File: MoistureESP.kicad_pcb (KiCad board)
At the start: 2 copper layers, 104 parts, among them J1 Conn_01x03_Pin, J2 Conn_MoisturePCB, J3 Conn_DS18B20, J4 USB4110-GF-A, J6 Conn_01x02_Pin, J7 Conn_01x06_Pin, Q1 SSM6K513NU-LF, Q10 DMP3068L-7, Q2 SSM6K513NU-LF, Q3 2N7002W, Q4 BC817W, Q5 BC817W, Q6 RUM002N05T2L, Q7 RUM002N05T2L, Q8 DMP3068L-7, Q9 DMP3068L-7, SW1 147873-1, U1 BQ28Z620DRZR, U2 ESP32-WROOM-32, U3 TPS7A2601DRVR, U4 TPS7A2601DRVR, U5 MAX77757JEFG420+

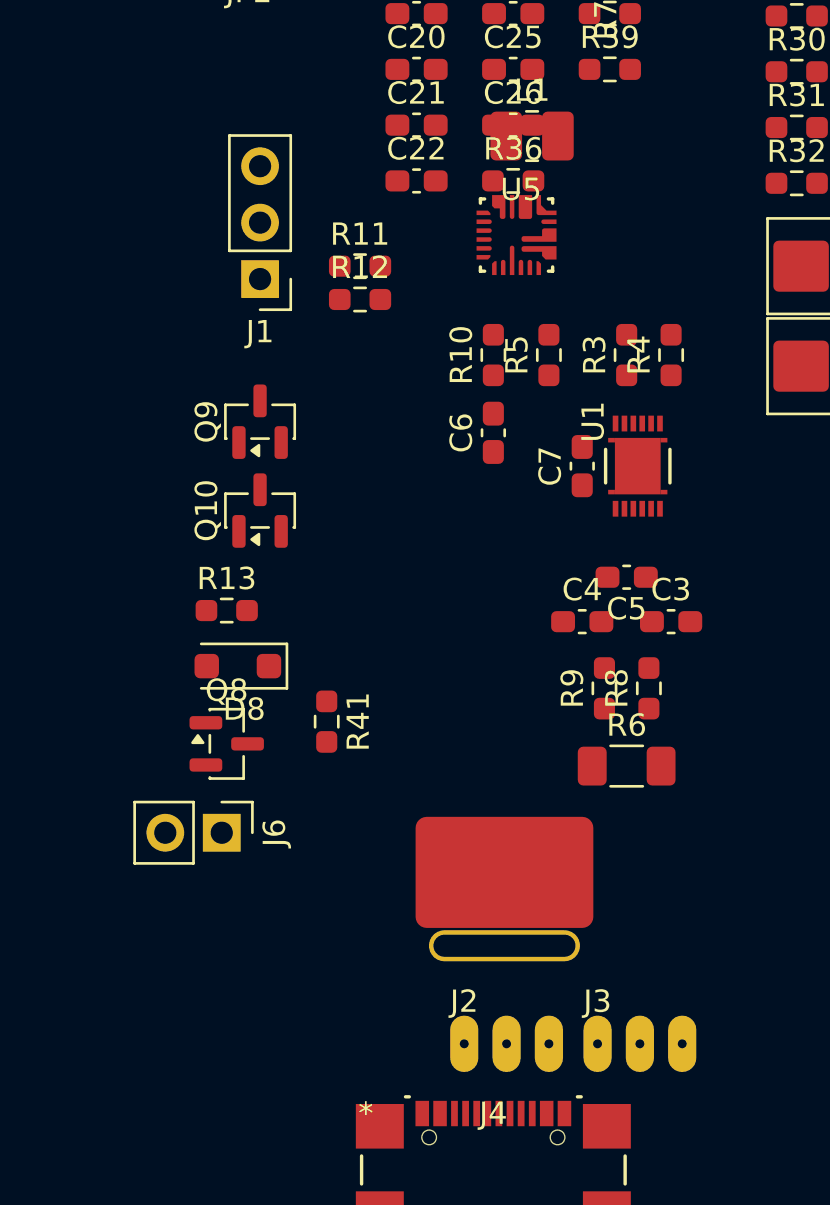
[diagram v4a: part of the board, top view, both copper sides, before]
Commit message: Change protection FETs and add resistor.
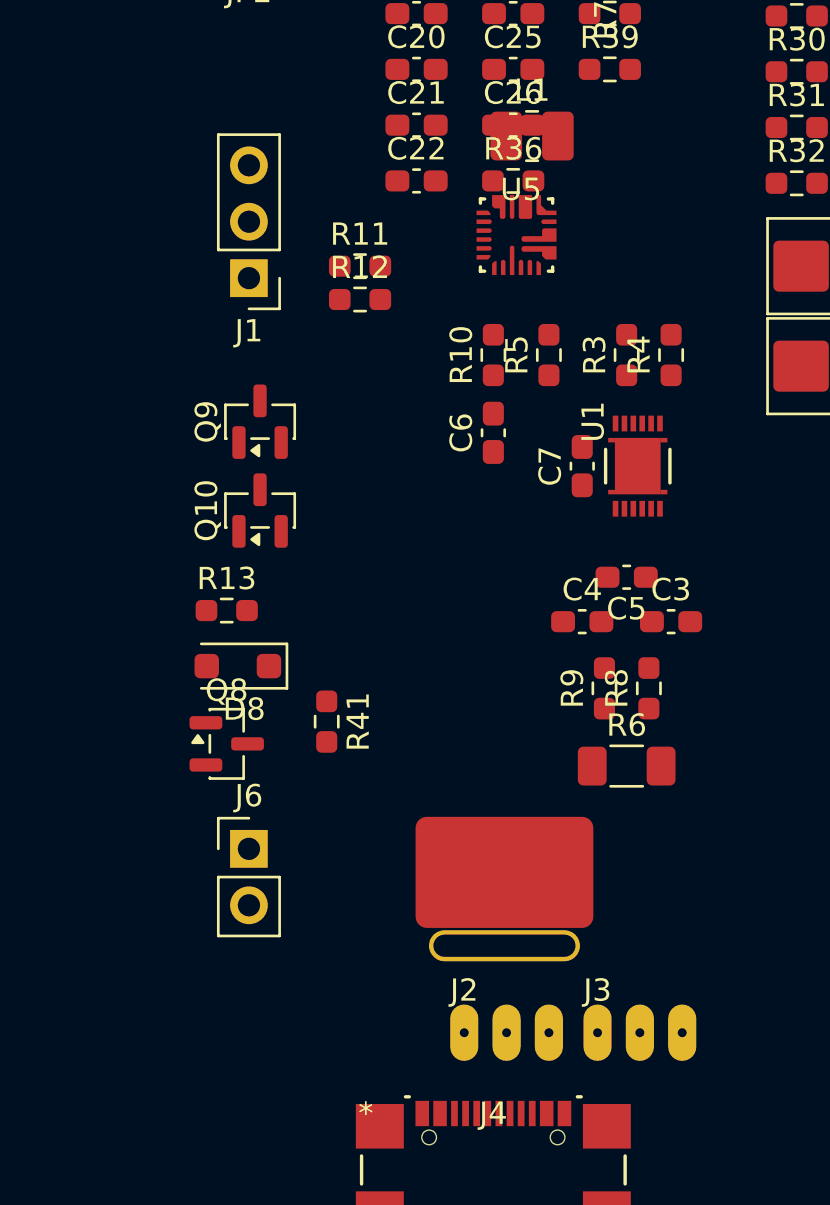
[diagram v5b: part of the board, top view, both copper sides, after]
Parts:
- moved J6 1.42 mm to (73.5, 125.7), turned to 0 degrees
- moved J1 0.50 mm to (73.5, 100.0)
- moved J2 0.50 mm to (83.2, 134.0)
- moved J3 0.50 mm to (89.2, 134.0)
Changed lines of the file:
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@@
 	(footprint "custom:sensorwirepads3x1"
 		(layer "F.Cu")
-		(at 83.19 134.5)
+		(at 83.19 134)
 		(property "Reference" "J2"
 			(at 0 -1.905 0)
@@
 	(footprint "Connector_PinHeader_2.54mm:PinHeader_1x02_P2.54mm_Vertical"
 		(layer "F.Cu")
-		(at 72.275 125 -90)
+		(at 73.5 125.725)
 		(descr "Through hole straight pin header, 1x02, 2.54mm pitch, single row")
 		(tags "Through hole pin header THT 1x02 2.54mm single row")
 		(property "Reference" "J6"
-			(at 0 -2.38 90)
+			(at 0 -2.38 0)
 			(layer "F.SilkS")
 			(effects
@@
 		)
 		(property "Value" "Conn_01x02_Pin"
-			(at 0 4.92 90)
+			(at 0 4.92 0)
 			(layer "F.Fab")
 			(effects
@@
 		)
 		(property "Datasheet" ""
-			(at 0 0 90)
+			(at 0 0 0)
 			(layer "F.Fab")
 			(hide yes)
@@
 		)
 		(property "Description" "Generic connector, single row, 01x02, script generated"
-			(at 0 0 90)
+			(at 0 0 0)
 			(layer "F.Fab")
 			(hide yes)
@@
 		)
 		(property "KiLib_Generator" "connector/pin_header_socket"
-			(at 0 0 90)
+			(at 0 0 0)
 			(layer "F.SilkS")
 			(hide yes)
@@
 		(duplicate_pad_numbers_are_jumpers no)
 		(fp_line
-			(start -1.38 3.92)
-			(end 1.38 3.92)
+			(start -1.38 -1.38)
+			(end 0 -1.38)
 			(stroke
 				(width 0.12)
@@
 		)
 		(fp_line
-			(start -1.38 1.27)
-			(end -1.38 3.92)
+			(start -1.38 0)
+			(end -1.38 -1.38)
 			(stroke
 				(width 0.12)
@@
 		(fp_line
 			(start -1.38 1.27)
-			(end 1.38 1.27)
+			(end -1.38 3.92)
 			(stroke
 				(width 0.12)
@@
 		)
 		(fp_line
-			(start 1.38 1.27)
-			(end 1.38 3.92)
+			(start -1.38 1.27)
+			(end 1.38 1.27)
 			(stroke
 				(width 0.12)
@@
 		)
 		(fp_line
-			(start -1.38 0)
-			(end -1.38 -1.38)
+			(start -1.38 3.92)
+			(end 1.38 3.92)
 			(stroke
 				(width 0.12)
@@
 		)
 		(fp_line
-			(start -1.38 -1.38)
-			(end 0 -1.38)
+			(start 1.38 1.27)
+			(end 1.38 3.92)
 			(stroke
 				(width 0.12)
@@
 		)
 		(fp_line
-			(start -1.27 3.81)
-			(end -1.27 -0.635)
+			(start -1.27 -0.635)
+			(end -0.635 -1.27)
 			(stroke
 				(width 0.1)
@@
 		)
 		(fp_line
-			(start 1.27 3.81)
-			(end -1.27 3.81)
+			(start -1.27 3.81)
+			(end -1.27 -0.635)
 			(stroke
 				(width 0.1)
@@
 		)
 		(fp_line
-			(start -1.27 -0.635)
-			(end -0.635 -1.27)
+			(start -0.635 -1.27)
+			(end 1.27 -1.27)
 			(stroke
 				(width 0.1)
@@
 		)
 		(fp_line
-			(start -0.635 -1.27)
-			(end 1.27 -1.27)
+			(start 1.27 -1.27)
+			(end 1.27 3.81)
 			(stroke
 				(width 0.1)
@@
 		)
 		(fp_line
-			(start 1.27 -1.27)
-			(end 1.27 3.81)
+			(start 1.27 3.81)
+			(end -1.27 3.81)
 			(stroke
 				(width 0.1)
@@
 		)
 		(fp_text user "${REFERENCE}"
-			(at 0 1.27 0)
+			(at 0 1.27 90)
 			(layer "F.Fab")
 			(effects
@@
 		)
 		(pad "1" thru_hole rect
-			(at 0 0 270)
+			(at 0 0)
 			(size 1.7 1.7)
 			(drill 1)
@@
 		)
 		(pad "2" thru_hole circle
-			(at 0 2.54 270)
+			(at 0 2.54)
 			(size 1.7 1.7)
 			(drill 1)
@@
 	(footprint "custom:sensorwirepads3x1"
 		(layer "F.Cu")
-		(at 89.19 134.5)
+		(at 89.19 134)
 		(property "Reference" "J3"
 			(at 0 -1.905 0)
@@
 	(footprint "Connector_PinHeader_2.54mm:PinHeader_1x03_P2.54mm_Vertical"
 		(layer "F.Cu")
-		(at 74 100.08 180)
+		(at 73.5 100.04 180)
 		(descr "Through hole straight pin header, 1x03, 2.54mm pitch, single row")
 		(tags "Through hole pin header THT 1x03 2.54mm single row")

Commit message: Placement concept is finished.
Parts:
- added D3: LED, LED_SMD:LED_0603_1608Metric, B.Cu at (97.0, 69.0)
- added D4: LED, LED_SMD:LED_0603_1608Metric, B.Cu at (95.0, 69.0)
- added R42: 10K, Resistor_SMD:R_0603_1608Metric_Pad0.98x0.95mm_HandSolder, F.Cu at (75.0, 117.5)
- D5, R35, R40: moved to F.Cu
- D6, D7: value SM6T6V8A -> ESD5Zxx; footprint Diode_SMD:D_SMB -> Diode_SMD:D_SOD-523
- Q10: value DMP3068L-7 -> BC856BLT1G0SCT-ND
- Q8, Q9: value DMP3068L-7 -> SI7137DP-T1-GE3; footprint Package_TO_SOT_SMD:SOT-23 -> custom:MOSFET_7DP-T1-GE3_VIS
- moved D2 37.6 mm to (73.4, 66.5), turned to 180 degrees
- moved R32 35.7 mm to (73.5, 70.0), turned to -90 degrees
- moved R31 33.5 mm to (78.0, 66.5), turned to -90 degrees
- moved D1 31.4 mm to (76.5, 69.5), turned to 180 degrees
- moved R36 30.9 mm to (92.0, 65.5)
- moved C16 30.3 mm to (77.0, 64.0)
- moved R30 28.6 mm to (77.0, 71.5)
- moved R29 24.7 mm to (78.0, 74.0), turned to -90 degrees
- moved J1 24.2 mm to (96.0, 109.1)
- moved D5 24.0 mm to (96.5, 65.5), turned to 0 degrees
- moved R40 23.5 mm to (96.5, 67.5), turned to 0 degrees
- moved R12 19.6 mm to (95.0, 111.5), turned to 180 degrees
- moved R35 19.5 mm to (93.5, 70.5)
- moved R37 18.3 mm to (92.0, 67.5)
- moved R11 17.8 mm to (93.5, 109.0), turned to -90 degrees
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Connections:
- Q10 pad 2: Net-(Q10-S) -> Net-(Q10-E)
- Q10 pad 3: Net-(Q10-D) -> Net-(Q10-C)
- Q8 pad 1: GNDPWR -> Net-(Q10-E)
- Q8 pad 2: Net-(Q10-S) -> Net-(Q8-S-Pad2)
- Q8 pad 3: /auxchgr_prot/Vin+ -> Net-(Q8-S-Pad2)
- Q9 pad 1: Net-(Q10-D) -> Net-(Q10-E)
- Q9 pad 2: Net-(Q10-S) -> Net-(Q9-S-Pad2)
- Q9 pad 3: /charger/VBat -> Net-(Q9-S-Pad2)
- R13 pad 2: Net-(Q10-D) -> Net-(Q10-C)
- R41 pad 2: Net-(Q10-S) -> Net-(Q10-E)
- U2 pad 10: /mcu/onewire_pin -> unconnected-(U2-IO25-Pad10)
- U2 pad 11: /mcu/analog_enable -> /mcu/Disp.SDA
- U2 pad 12: unconnected-(U2-IO27-Pad12) -> /mcu/Disp.SCL
- U2 pad 23: /mcu/Disp.SDA -> /mcu/analog_enable
- U2 pad 24: /mcu/Disp.SCL -> /mcu/onewire_pin

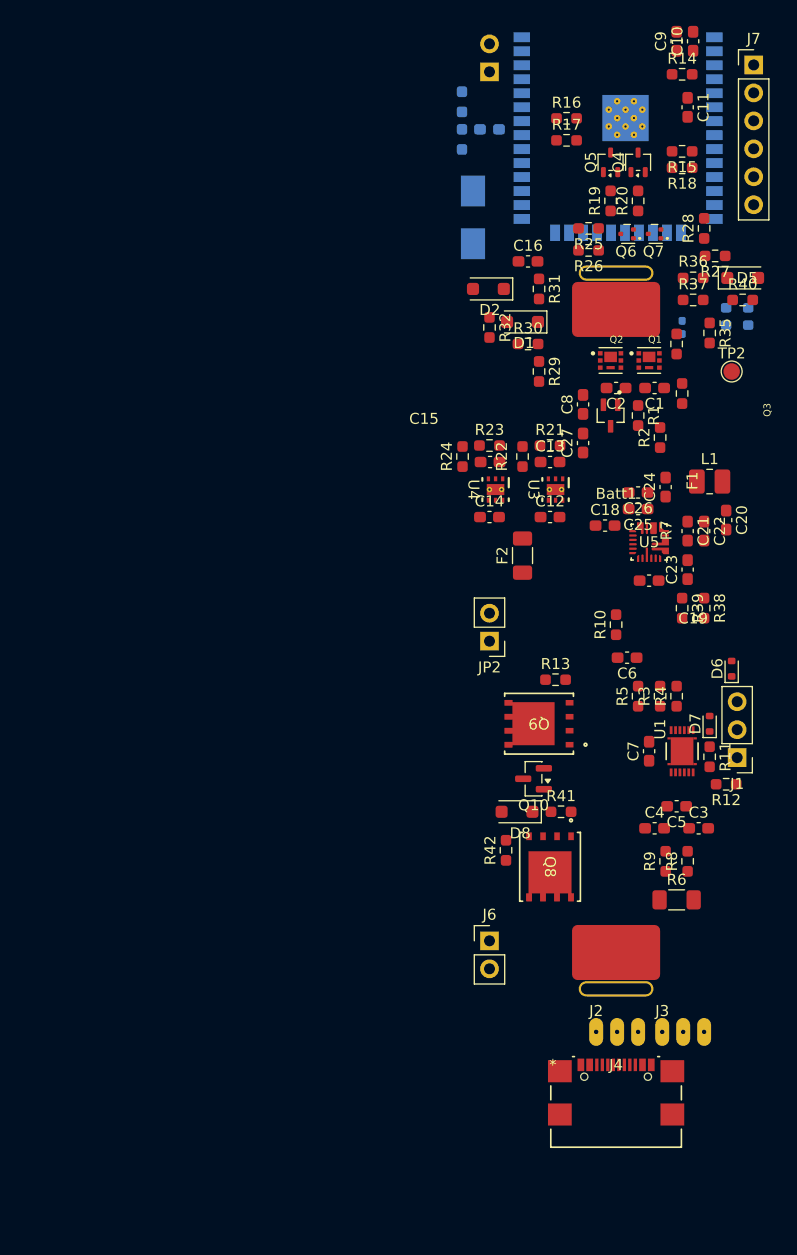
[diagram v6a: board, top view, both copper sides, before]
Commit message: Add wiring, change footprint to avoid fatal errors at pads.
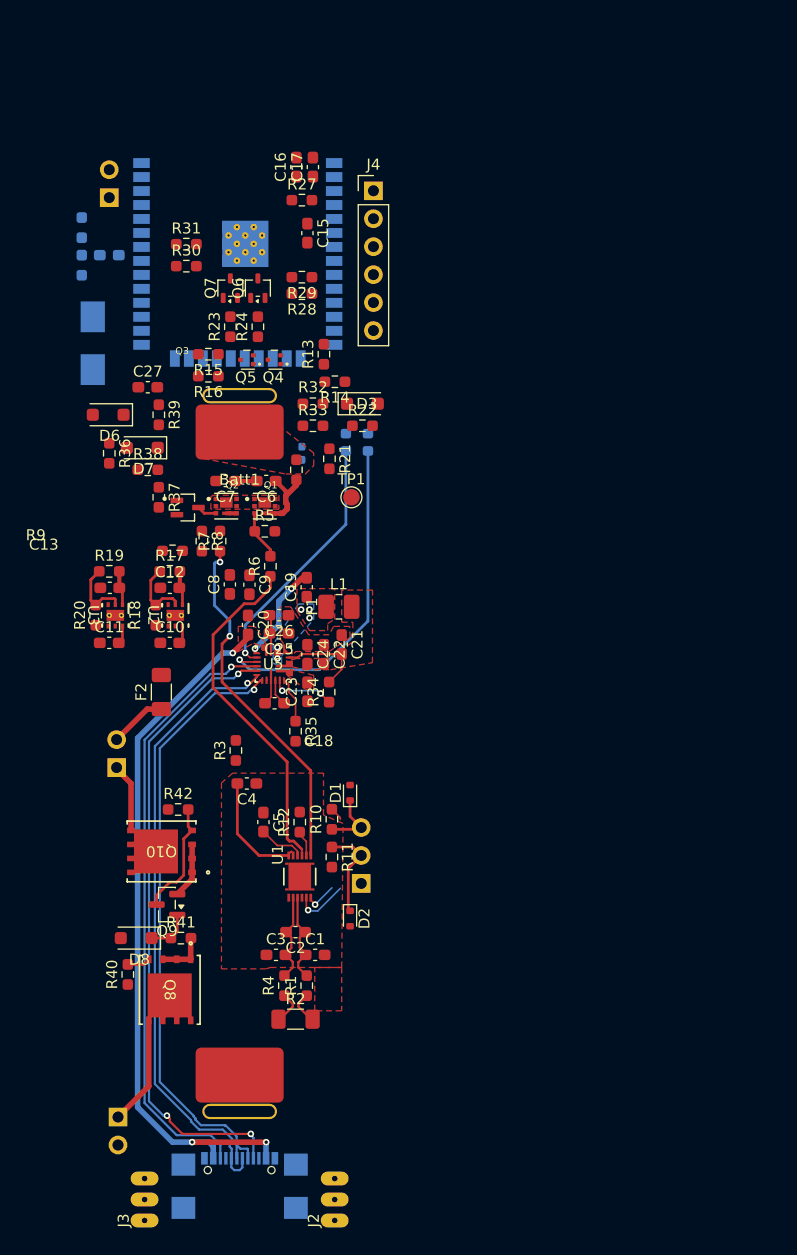
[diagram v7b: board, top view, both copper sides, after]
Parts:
- removed the Q9 at (78.0, 106.0)
- added Q10: SI7137DP-T1-GE3, custom:MOSFET_7DP-T1-GE3_VIS, F.Cu at (43.7, 117.6)
- J1: renamed from J6; moved to B.Cu
- J5: renamed from J1; moved to B.Cu
- J7: renamed from J4; moved to B.Cu
- JP1: renamed from JP2; moved to B.Cu
- moved J3 50.0 mm to (42.2, 151.1), turned to 90 degrees
- moved R9 48.5 mm to (44.7, 90.3), turned to 0 degrees
- moved R7 43.8 mm to (49.0, 89.4)
- moved R8 42.7 mm to (47.4, 89.4), turned to -90 degrees
- moved Q3 39.3 mm to (46.1, 86.4), turned to 0 degrees
- moved R35 38.8 mm to (55.9, 106.7)
- moved J1 37.4 mm to (39.8, 141.7), turned to 180 degrees
- moved Q1 37.3 mm to (53.1, 86.2)
- moved Q2 37.3 mm to (49.6, 86.2)
- moved R6 37.3 mm to (53.6, 91.7)
- moved D2 37.2 mm to (60.8, 123.7), turned to -90 degrees
- moved C21 36.7 mm to (60.1, 98.8)
- moved C1 36.7 mm to (57.7, 127.0)
- moved U1 36.6 mm to (56.3, 119.9)
- moved C7 36.5 mm to (49.5, 83.9)
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- renumbered C3 to C1, C12 to C10, C14 to C11, C13 to C12, C15 to C13, C17 to C14, C11 to C15, C9 to C16, C10 to C17, C19 to C18, C24 to C19, C5 to C2, C18 to C20, C20 to C21, C21 to C24, C16 to C27, C4 to C3, C6 to C4, C7 to C5, C1 to C6, C2 to C7, C27 to C9, D6 to D1, D7 to D2, D5 to D3, D3 to D4, D4 to D5, D2 to D6, D1 to D7, J7 to J4, JP1 to JP2, Q7 to Q4, Q6 to Q5, Q4 to Q6, Q5 to Q7, Q10 to Q9, R8 to R1, R11 to R10, R12 to R11, R5 to R12, R28 to R13, R27 to R14, R25 to R15, R26 to R16, R21 to R17, R22 to R18, R23 to R19, R6 to R2, R24 to R20, R35 to R21, R40 to R22, R19 to R23, R20 to R24, R33 to R25, R34 to R26, R14 to R27, R18 to R28, R15 to R29, R10 to R3, R17 to R30, R16 to R31, R36 to R32, R37 to R33, R39 to R34, R38 to R35, R32 to R36, R29 to R37, R30 to R38, R31 to R39, R9 to R4, R42 to R40, R13 to R42, R1 to R5, R3 to R6, R4 to R7, R2 to R8, R7 to R9, TP2 to TP1, U3 to U2, U4 to U3, U2 to U4
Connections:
- C19 pad 1: Net-(C24-Pad1) -> Net-(C19-Pad1)
- L1 pad 1: Net-(C24-Pad1) -> Net-(C19-Pad1)
- Q8 pad 1: Net-(Q10-E) -> Net-(Q9-E)
- Q8 pad 2: Net-(Q8-S-Pad2) -> Net-(Q9-E)
- Q8 pad 3: Net-(Q8-S-Pad2) -> Net-(Q9-E)
- Q8 pad 6: Net-(Q8-D-Pad6) -> /auxchgr_prot/Vin+
- Q8 pad 7: Net-(Q8-D-Pad6) -> /auxchgr_prot/Vin+
- Q8 pad 8: Net-(Q8-D-Pad6) -> /auxchgr_prot/Vin+
- Q9 pad 2: Net-(Q10-E) -> Net-(Q9-E)
- R41 pad 2: Net-(Q10-E) -> Net-(Q9-E)
- U5 pad 20: Net-(C24-Pad1) -> Net-(C19-Pad1)
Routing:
- net VBUS: track 0.00 -> 65.3 mm, vias 0 -> 3
- net /charger/CC1: track 0.00 -> 58.1 mm, vias 0 -> 3
- net /charger/DP1: track 0.00 -> 57.4 mm, vias 0 -> 1
- net /charger/DN1: track 0.00 -> 56.0 mm, vias 0 -> 1
- net /charger/CC2: track 0.00 -> 55.8 mm, vias 0 -> 1
- net Net-(U1-DSG): track 0.00 -> 32.3 mm, vias 0 -> 2
- net Net-(U1-CHG): track 0.00 -> 31.7 mm
- net Net-(D4-K): track 0.00 -> 31.0 mm, vias 0 -> 1
- net /charger/~{INOK}: track 0.00 -> 23.4 mm, vias 0 -> 1
- net Net-(U1-VC1): track 0.00 -> 11.0 mm
- net Net-(Q10-G): track 0.00 -> 10.5 mm
- net /auxchgr_prot/Vin+: track 0.00 -> 9.94 mm
- net Net-(Q9-E): track 0.00 -> 9.54 mm
- net Net-(U5-BST): track 0.00 -> 9.11 mm, vias 0 -> 2
- net /battery/comm.SDA: track 0.00 -> 8.73 mm
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- added copper zone on F.Cu, net /battery/Vcell+
- added copper zone on F.Cu, net /charger/VBat
- added copper zone on F.Cu, net CGND
- added copper zone on F.Cu, net GNDPWR
- added copper zone on B.Cu, net Net-(C19-Pad1)
- added copper zone on F.Cu, net Net-(C19-Pad1)
- added copper zone on F.Cu, net Net-(Q1-Pad1)
- added copper zone on F.Cu, net VBUS
- added copper zone on F.Cu, net Vsys

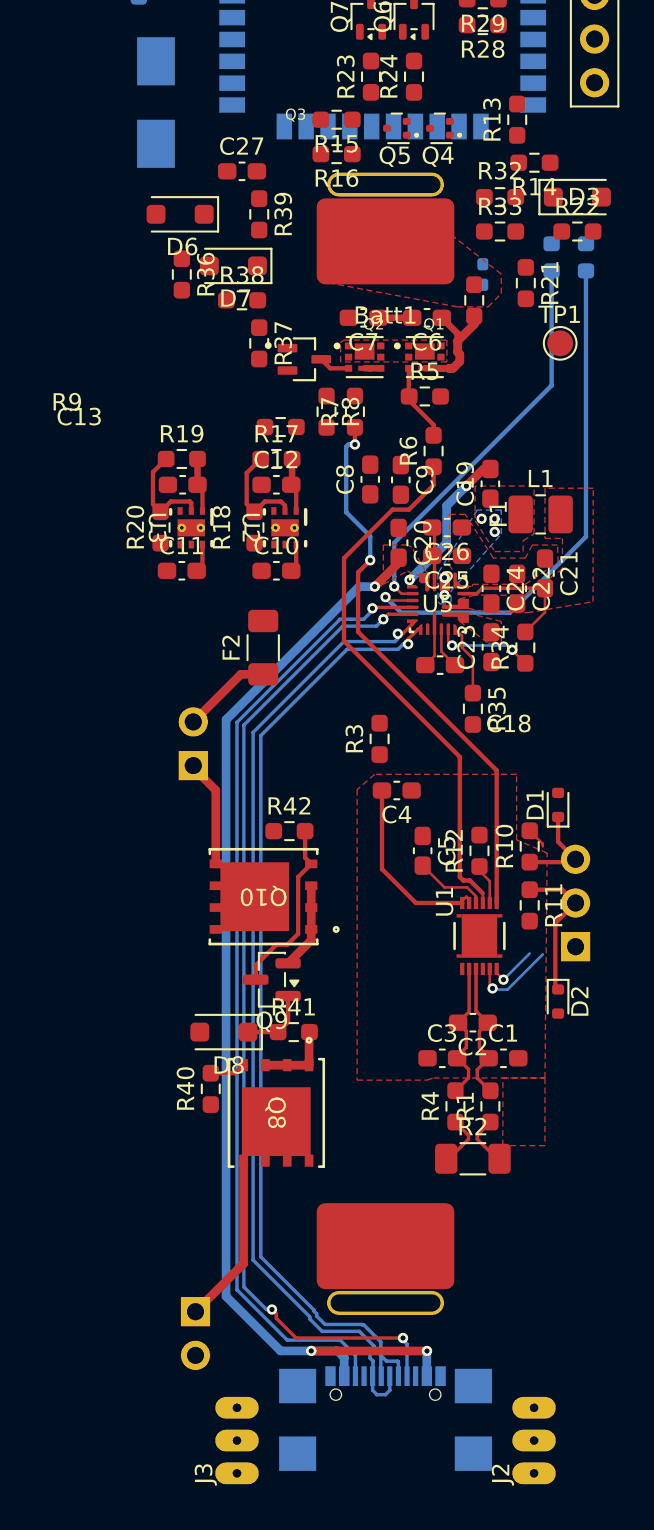
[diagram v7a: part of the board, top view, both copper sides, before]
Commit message: Add VBAT polygon, add BQ control wiring.
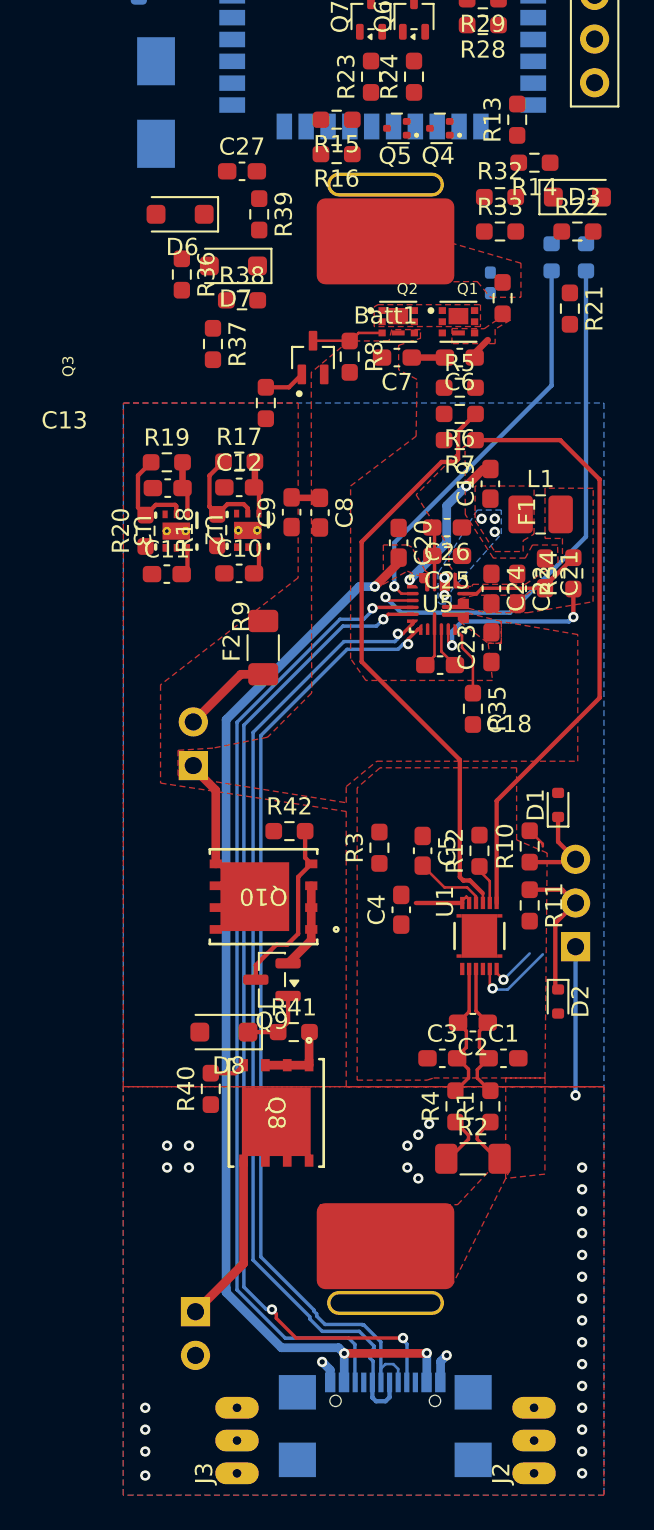
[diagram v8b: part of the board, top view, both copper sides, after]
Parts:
- removed TP1: TestPoint, TestPoint:TestPoint_Pad_D1.5mm
- moved C4 6.94 mm to (51.7, 118.4), turned to 90 degrees
- moved C9 6.62 mm to (45.3, 95.2), turned to 90 degrees
- moved R3 6.33 mm to (50.4, 114.8)
- moved R7 6.32 mm to (55.1, 91.1), turned to 180 degrees
- moved R34 5.14 mm to (61.7, 98.8)
- moved C8 3.50 mm to (47.0, 95.3), turned to -90 degrees
- moved R8 3.47 mm to (48.7, 86.2)
- moved C7 3.01 mm to (51.5, 86.3)
- moved C6 3.00 mm to (55.1, 86.3)
- moved R21 2.96 mm to (61.5, 83.4)
- moved Q1 2.84 mm to (55.0, 84.2)
- moved Q2 2.84 mm to (51.5, 84.2)
- moved R37 2.69 mm to (40.8, 85.5)
- moved R6 2.64 mm to (55.1, 89.5), turned to 180 degrees
- moved C10 2.17 mm to (42.3, 98.8)
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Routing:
- net GNDPWR: track 3.08 -> 14.5 mm, vias 0 -> 3
- net Net-(U1-VC1): track 11.0 -> 3.60 mm
- net Net-(C6-Pad1): track 7.67 -> 1.34 mm
- net Net-(U5-THM): track 5.75 -> 10.9 mm
- net Net-(Q1-Pad3): track 4.50 -> 0.00 mm
- net Net-(U1-CHG): track 31.7 -> 34.8 mm
- net Net-(U1-DSG): track 32.3 -> 35.3 mm, vias 2 -> 0
- net Net-(Q2-Pad3): track 1.80 -> 4.22 mm
- net Net-(Q3-Pad1): track 0.00 -> 2.40 mm
- net VBUS: track 65.3 -> 63.5 mm
- net Net-(C8-Pad1): track 0.00 -> 1.66 mm
- net /charger/DP1: track 57.4 -> 58.5 mm
- net /charger/VBat: track 7.19 -> 6.26 mm
- net /charger/CC2: track 55.8 -> 56.5 mm
- net /charger/PVL: track 7.91 -> 7.36 mm
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- added copper zone on B.Cu, net GNDPWR
- added copper zone on F.Cu, net Net-(C6-Pad1)
